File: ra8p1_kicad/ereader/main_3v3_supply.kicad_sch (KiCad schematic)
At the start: 20 parts, among them Q3 DMN2056U-7, U13 TPS63806YFFR, U16 74LVC1G17GW,125

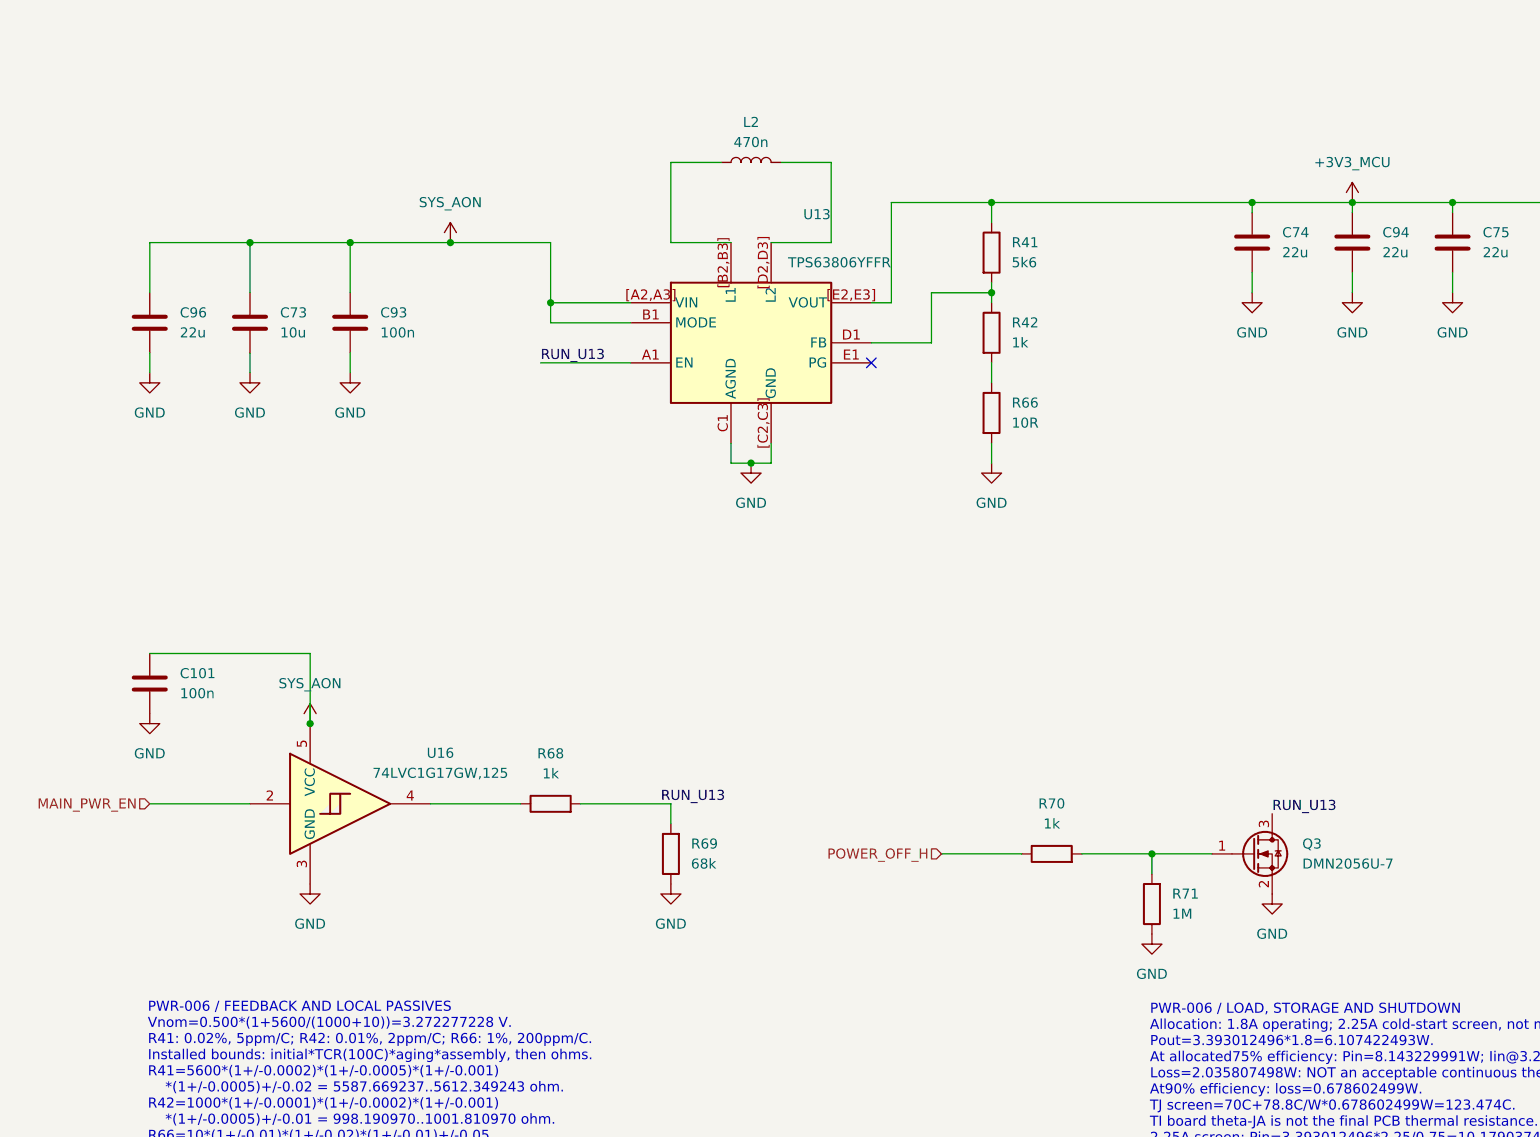
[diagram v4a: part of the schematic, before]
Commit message: wip(hardware): preserve schematic cleanup and CEU host ports
Checkpoint cosmetic cleanup across the schematic hierarchy and eleven parallel-camera host ports. Refresh the complete 13-page PDF. All 334 existing net partitions and 271 component records match the prior CEU checkpoint; all 128 ERC identities remain unchanged. Electrical design is incomplete; this is a WIP checkpoint for #821 and #841.
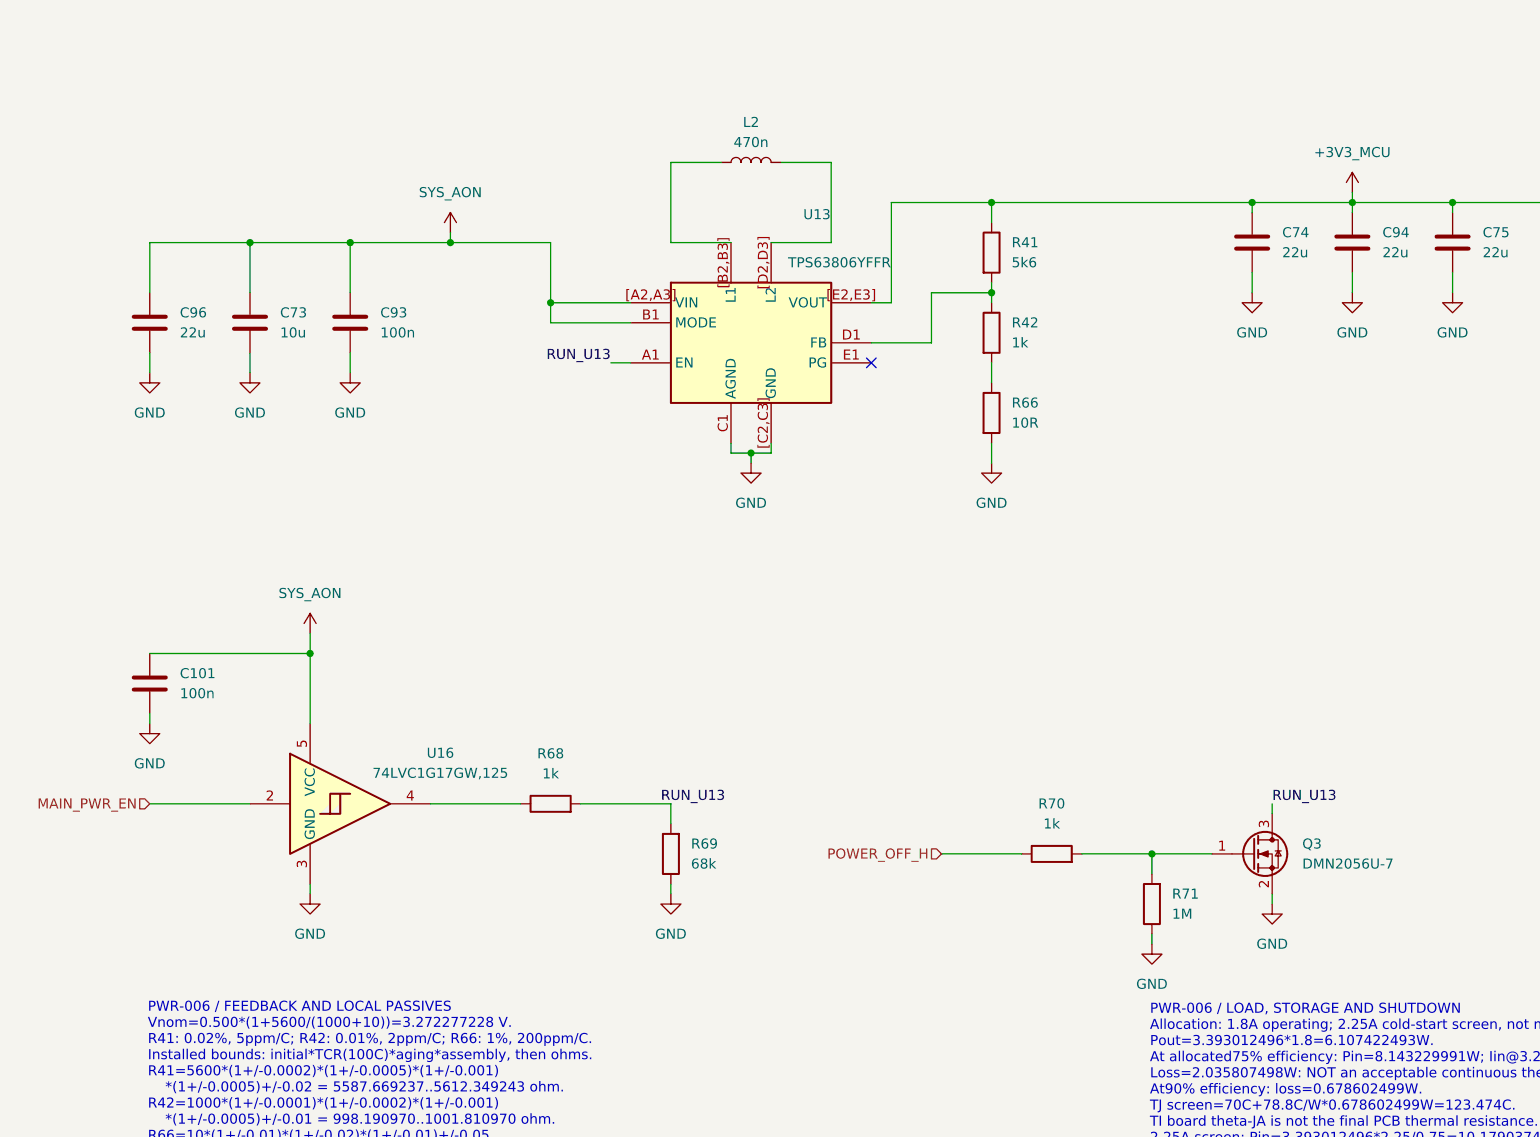
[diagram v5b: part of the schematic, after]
